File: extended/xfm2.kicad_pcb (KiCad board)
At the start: 2 copper layers, 178.1 x 70.6 mm, 63 parts, among them J1 Midi In, J2 Pin Breakout, J3 Midi Out, J4 Midi Thru, J5 Conn_Coaxial, J6 Jack-DC, J7 A-100_Bus_Connector, J8 AudioJack2, J9 AudioJack2, U1 H11L1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

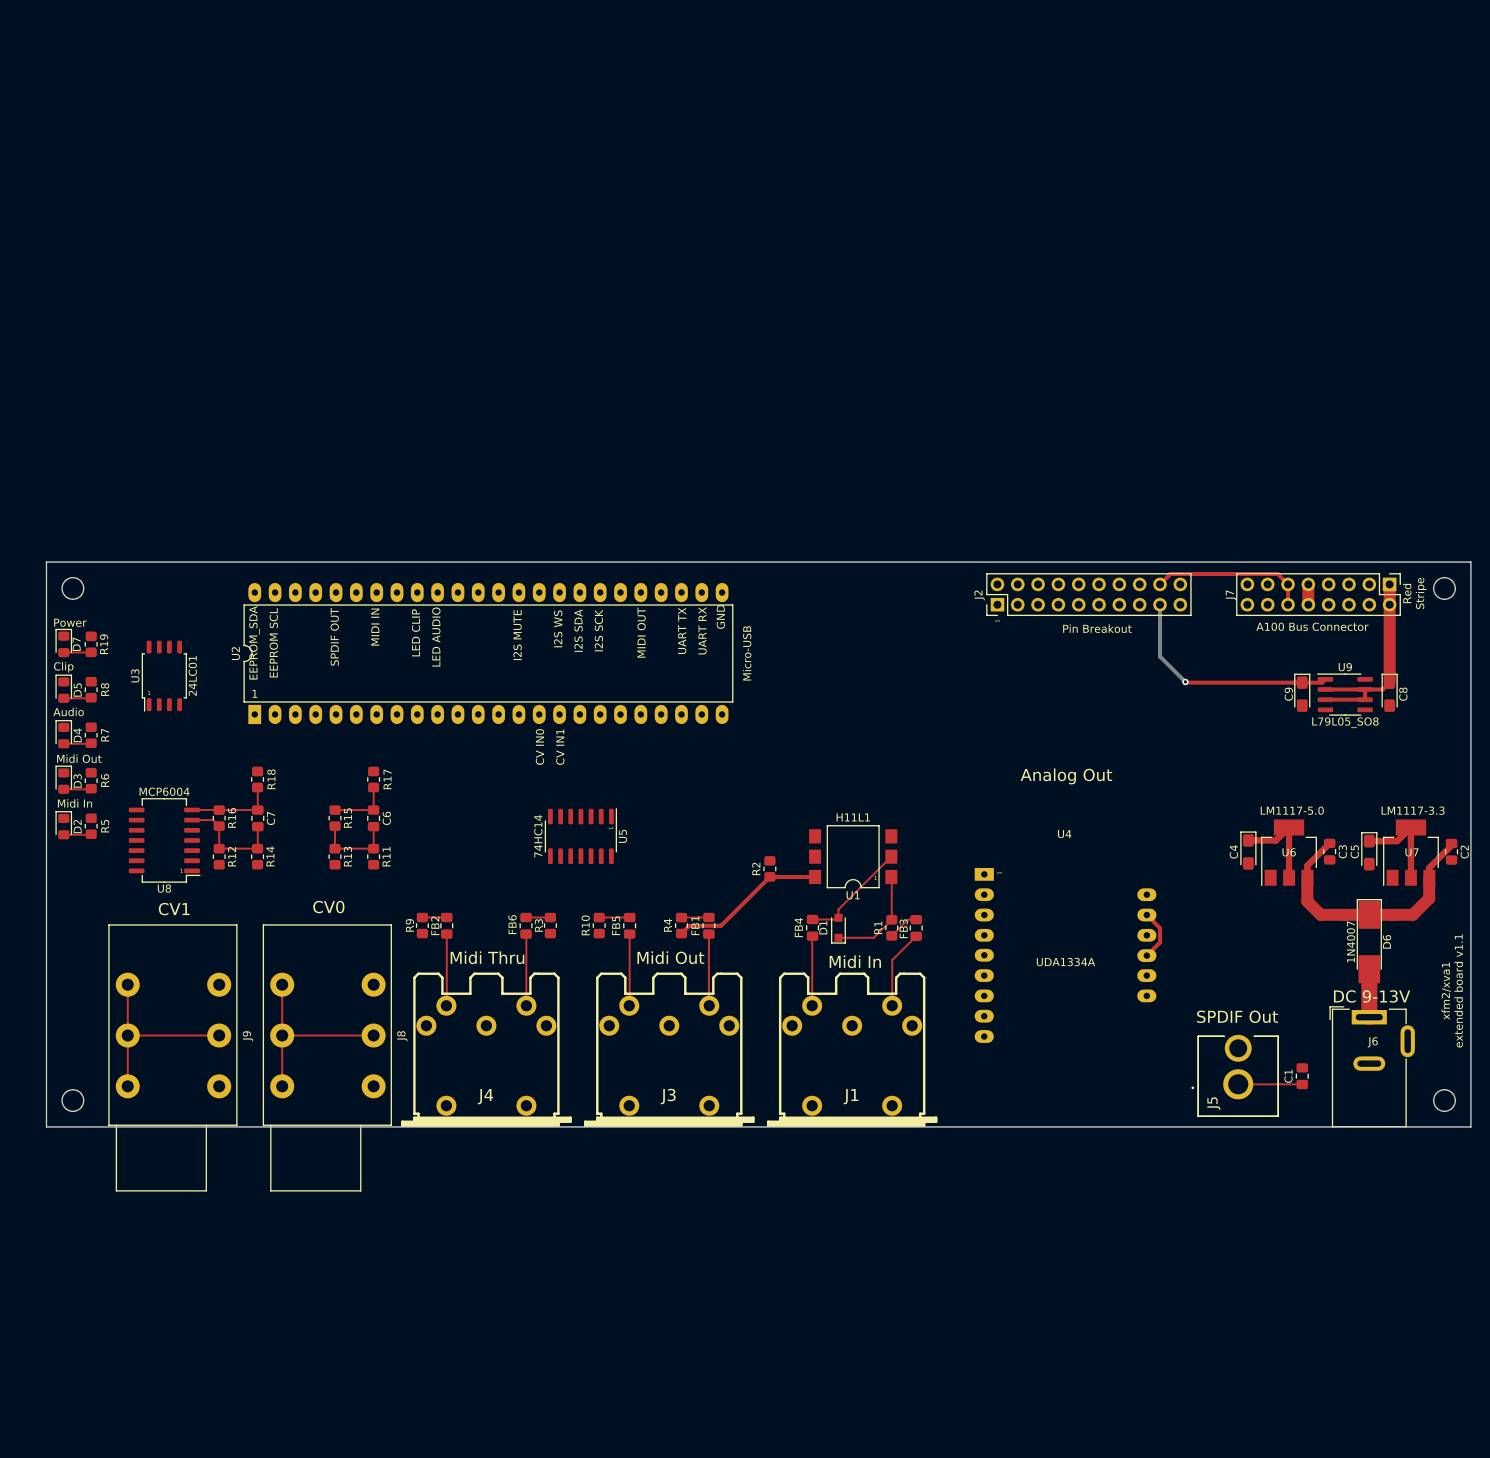
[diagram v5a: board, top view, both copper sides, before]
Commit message: fitted the 6.35mm audio jack which was too small. Added gerbers. ERC seems fine.
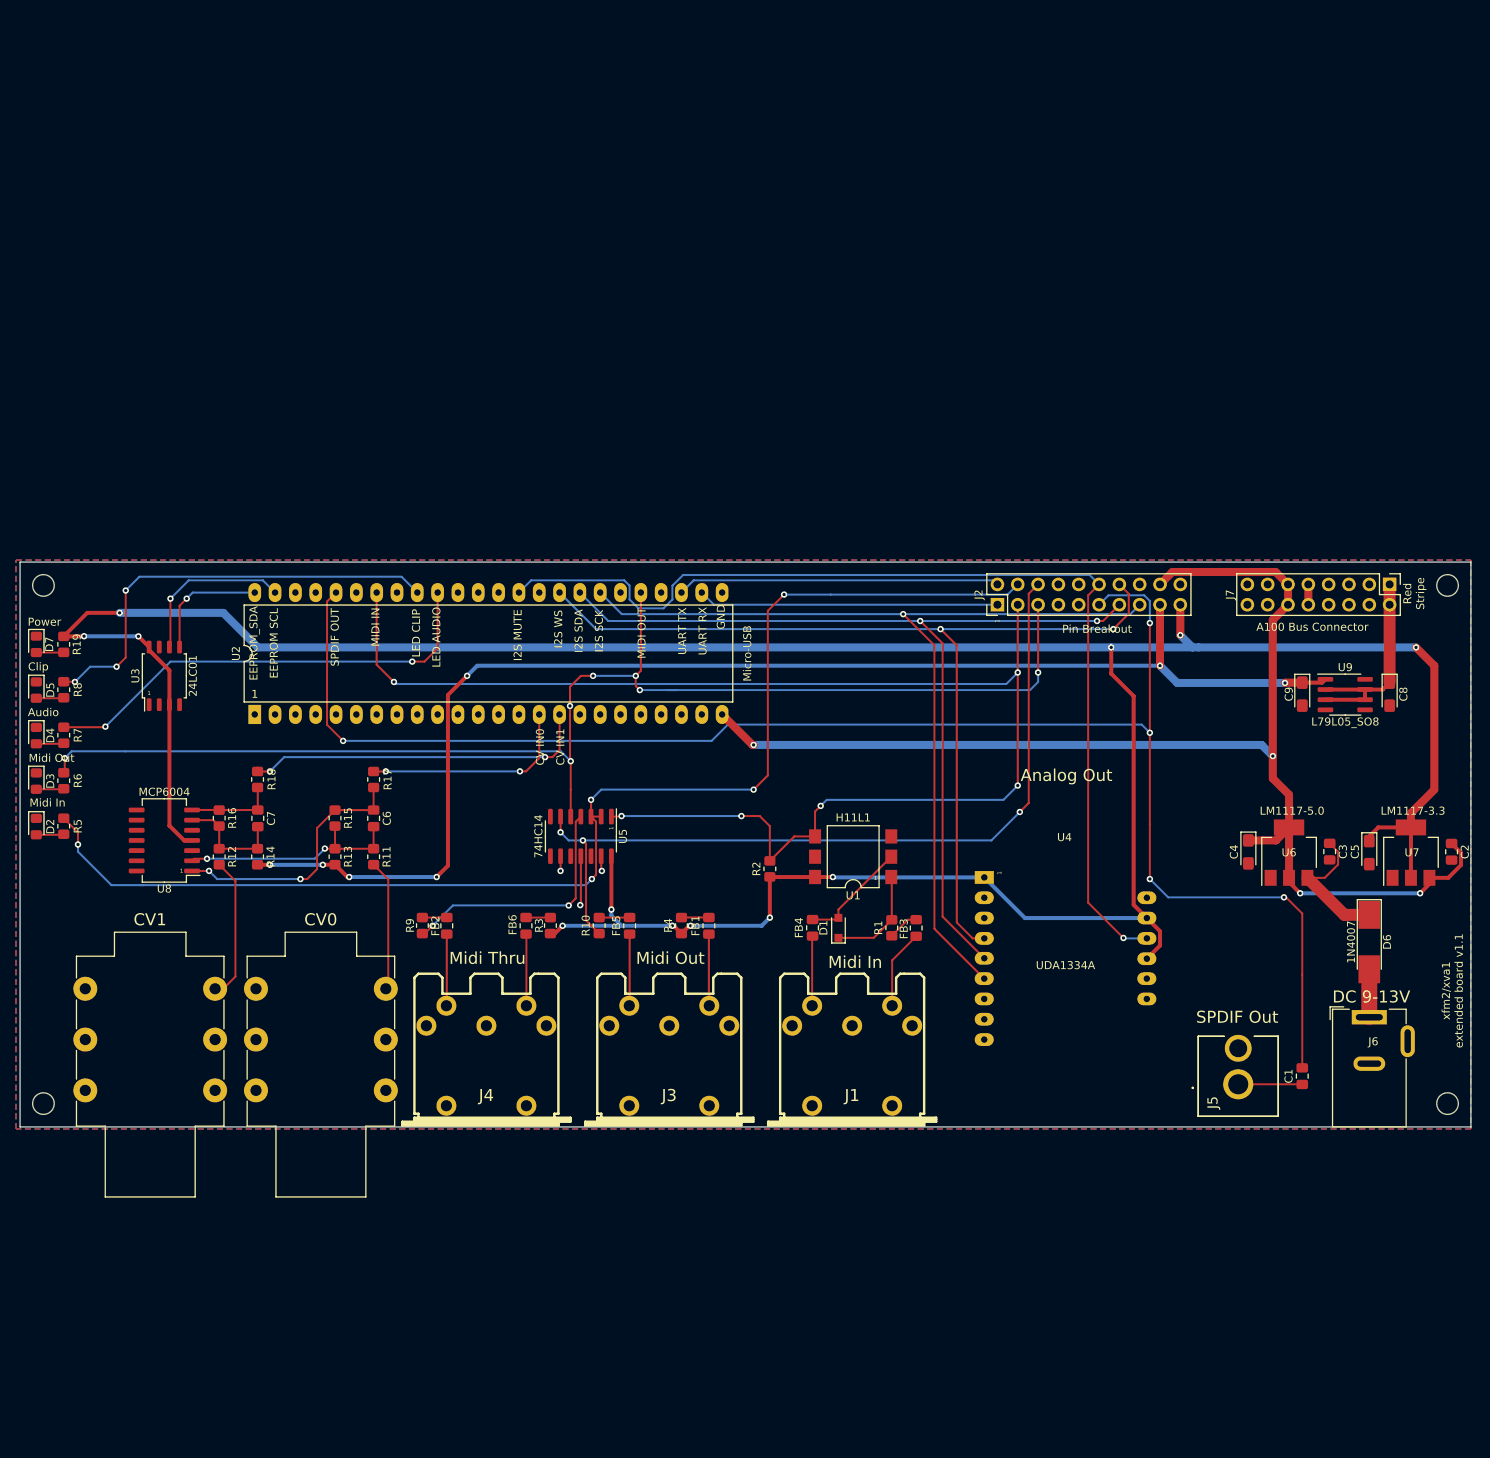
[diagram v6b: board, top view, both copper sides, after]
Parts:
- removed the REF** at (239.5, 87.4)
- removed the REF** at (239.5, 151.4)
- removed the REF** at (68.1, 151.4)
- removed the REF** at (68.1, 87.4)
- added REF**: MountingHole_2.7mm_M2.5_ISO7380, MountingHole:MountingHole_2.7mm_M2.5_ISO7380, F.Cu at (239.9, 87.0)
- added REF**: MountingHole_2.7mm_M2.5_ISO7380, MountingHole:MountingHole_2.7mm_M2.5_ISO7380, F.Cu at (239.9, 151.8)
- added REF**: MountingHole_2.7mm_M2.5_ISO7380, MountingHole:MountingHole_2.7mm_M2.5_ISO7380, F.Cu at (64.4, 151.8)
- added REF**: MountingHole_2.7mm_M2.5_ISO7380, MountingHole:MountingHole_2.7mm_M2.5_ISO7380, F.Cu at (64.4, 87.0)
- D7: value LED_CLIP -> LED_POWER
- J8, J9: footprint Connector_Audio:Jack_6.35mm_Neutrik_NRJ6HM-1_Horizontal -> xfm2:Jack_6.35mm_Neutrik_NMJ6HFD2_Horizontal-ST-only
- moved D2 3.43 mm to (63.5, 117.1)
- moved D3 3.43 mm to (63.5, 111.5)
- moved D4 3.43 mm to (63.5, 105.8)
- moved D5 3.43 mm to (63.5, 100.1)
- moved D7 3.43 mm to (63.5, 94.4)
- moved R19 3.43 mm to (66.9, 94.4)
- moved R5 3.43 mm to (66.9, 117.1)
- moved R6 3.43 mm to (66.9, 111.4)
- moved R7 3.43 mm to (66.9, 105.7)
- moved R8 3.43 mm to (66.9, 100.0)
- moved J8 1.61 mm to (107.2, 137.4)
- moved J9 0.72 mm to (85.9, 137.4)
- moved U4 0.38 mm to (182.0, 118.4)
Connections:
- C2 pad 1: Net-(C2-Pad1) -> +5V
- C3 pad 1: Net-(C2-Pad1) -> Net-(C3-Pad1)
- D6 pad 1: Net-(C2-Pad1) -> Net-(C3-Pad1)
- J8 pad S: Net-(J8-PadS) -> GND
- J8 pad T: GND -> Net-(J8-PadT)
- J9 pad S: Net-(J9-PadS) -> GND
- J9 pad T: GND -> Net-(J9-PadT)
- R11 pad 2: Net-(J8-PadS) -> Net-(J8-PadT)
- R12 pad 2: Net-(J9-PadS) -> Net-(J9-PadT)
- U6 pad 3: Net-(C2-Pad1) -> Net-(C3-Pad1)
- U7 pad 3: Net-(C2-Pad1) -> +5V
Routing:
- net +3V3: track 38.3 -> 388.4 mm, vias 0 -> 12
- net SPDIF_OUT: track 0.00 -> 204.0 mm, vias 0 -> 5
- net MIDI_IN: track 0.00 -> 174.8 mm, vias 0 -> 6
- net MIDI_OUT: track 0.00 -> 164.6 mm, vias 0 -> 7
- net MIDI_IN_INV: track 0.00 -> 159.9 mm, vias 0 -> 5
- net -5V: track 28.7 -> 166.3 mm, vias 1 -> 7
- net +5V: track 31.7 -> 160.6 mm, vias 0 -> 4
- net I2S_MUTE: track 0.00 -> 128.4 mm, vias 0 -> 1
- net I2S_WS: track 0.00 -> 119.8 mm, vias 0 -> 2
- net I2S_SCK: track 0.00 -> 118.8 mm, vias 0 -> 1
- net I2S_SDA: track 0.00 -> 115.2 mm, vias 0 -> 2
- net MIDI_OUT_INV: track 0.00 -> 103.1 mm, vias 0 -> 3
- net LED_AUDIO: track 0.00 -> 57.8 mm, vias 0 -> 2
- net LED_CLIP: track 0.00 -> 55.4 mm, vias 0 -> 3
- net (no net): track 48.3 -> 0.00 mm
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- added copper zone on B.Cu, net GND
- added copper zone on F.Cu, net GND
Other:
- board size 178.1 x 70.6 mm -> 181.4 x 70.6 mm

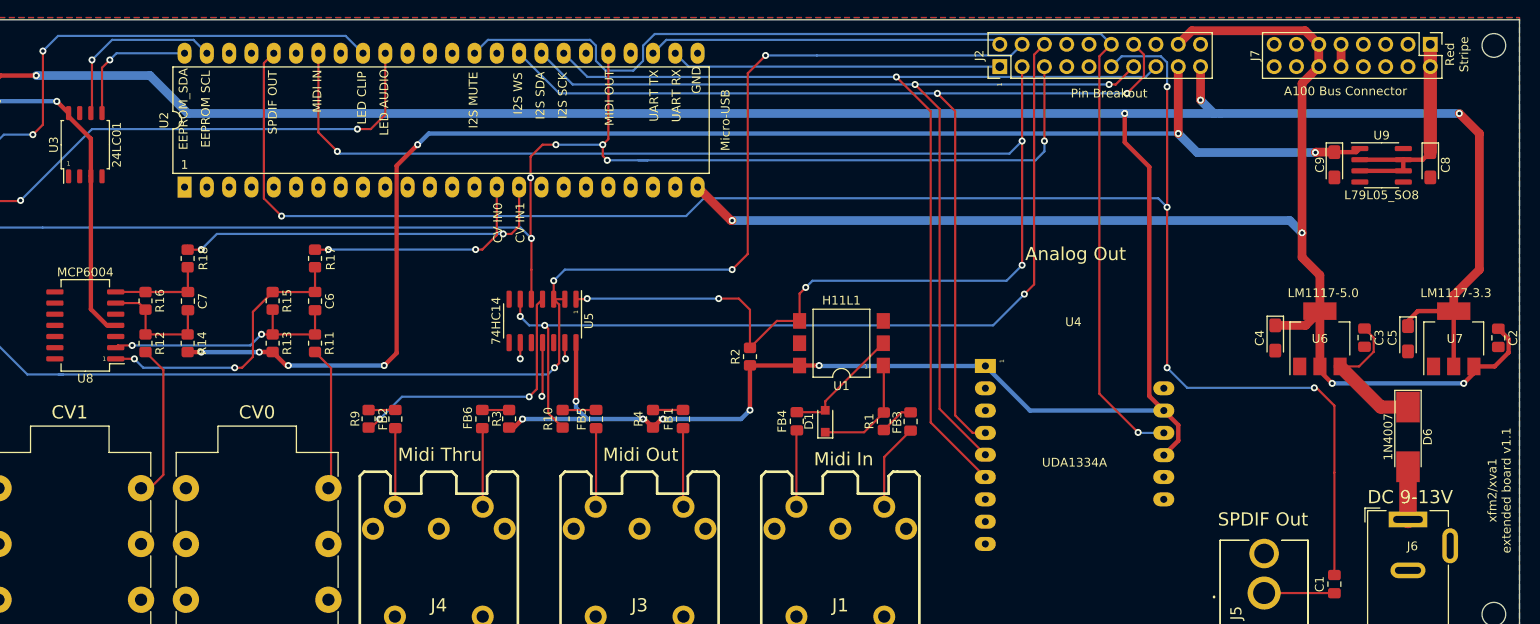
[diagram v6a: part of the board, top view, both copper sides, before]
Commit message: updates for the extended xfm2 board: replacement of opamp components, logic level converter 5v<->3.3v and pull ups for uart.
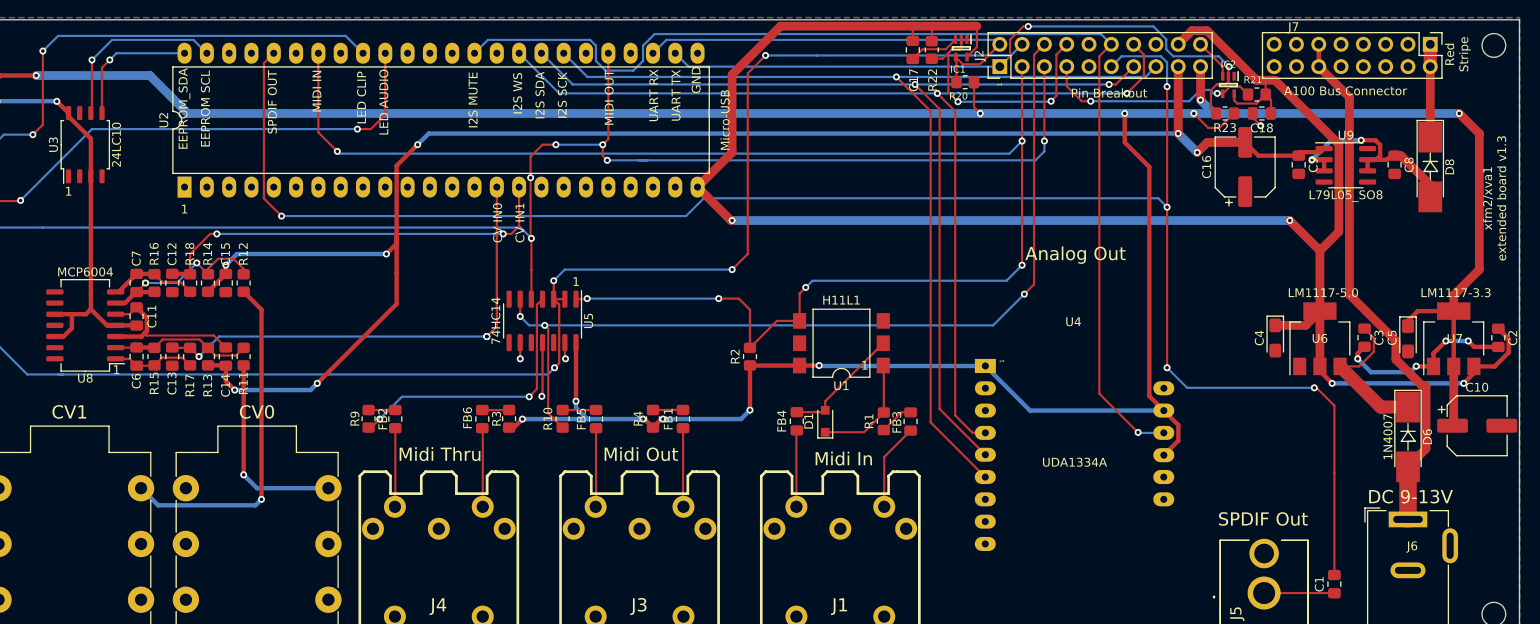
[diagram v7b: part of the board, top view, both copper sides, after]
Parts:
- added C10: 47uF, Capacitor_SMD:CP_Elec_6.3x5.4, F.Cu at (238.0, 130.3)
- added C11: 100nF, Capacitor_SMD:C_0805_2012Metric_Pad1.18x1.45mm_HandSolder, F.Cu at (85.3, 117.9)
- added C12: 100pF, Capacitor_SMD:C_0805_2012Metric_Pad1.18x1.45mm_HandSolder, F.Cu at (89.4, 114.0)
- added C13: 100pF, Capacitor_SMD:C_0805_2012Metric_Pad1.18x1.45mm_HandSolder, F.Cu at (89.4, 122.4)
- added C14: 0.1uF, Capacitor_SMD:C_0805_2012Metric_Pad1.18x1.45mm_HandSolder, F.Cu at (95.5, 122.4)
- added C15: 0.1uF, Capacitor_SMD:C_0805_2012Metric_Pad1.18x1.45mm_HandSolder, F.Cu at (95.5, 114.0)
- added C16: 47uF, Capacitor_SMD:CP_Elec_6.3x5.4, F.Cu at (211.6, 100.8)
- added C17: 100nF, Capacitor_SMD:C_0805_2012Metric_Pad1.18x1.45mm_HandSolder, F.Cu at (173.7, 87.5)
- added C18: 100nF, Capacitor_SMD:C_0805_2012Metric_Pad1.18x1.45mm_HandSolder, F.Cu at (213.5, 94.7)
- added D8: 1N4007, Diode_SMD:D_MELF_Handsoldering, F.Cu at (232.7, 100.8)
- added IC1: 74LVC1G07QSE-7, samacsys:SOT65P210X110-5N, F.Cu at (179.3, 87.3)
- added IC2: 74LVC1G07QSE-7, samacsys:SOT65P210X110-5N, F.Cu at (209.7, 91.5)
- added R20: 10k, Resistor_SMD:R_0805_2012Metric_Pad1.20x1.40mm_HandSolder, F.Cu at (179.7, 91.2)
- added R21: 10k, Resistor_SMD:R_0805_2012Metric_Pad1.20x1.40mm_HandSolder, F.Cu at (212.9, 92.6)
- added R22: 10k, Resistor_SMD:R_0805_2012Metric_Pad1.20x1.40mm_HandSolder, F.Cu at (175.9, 87.5)
- added R23: 10k, Resistor_SMD:R_0805_2012Metric_Pad1.20x1.40mm_HandSolder, F.Cu at (209.3, 94.7)
- C8, C9: footprint Capacitor_Tantalum_SMD:CP_EIA-3216-18_Kemet-A_Pad1.58x1.35mm_HandSolder -> Capacitor_SMD:C_0805_2012Metric_Pad1.18x1.45mm_HandSolder
- D1: value D -> 1N4148
- U3: value 24LC01 -> 24LC10
- moved C6 21.3 mm to (85.3, 122.4), turned to 90 degrees
- moved R17 18.1 mm to (91.4, 122.4)
- moved R15 14.9 mm to (87.4, 122.4), turned to 90 degrees
- moved R12 13.1 mm to (97.5, 114.0)
- moved R11 8.27 mm to (97.5, 122.4)
- moved R13 7.52 mm to (93.5, 122.4)
- moved R14 7.24 mm to (93.5, 114.0)
- moved C7 6.20 mm to (85.3, 114.0)
- moved C8 4.06 mm to (228.6, 100.6)
- moved C9 4.06 mm to (217.7, 100.6)
- moved U9 4.06 mm to (223.1, 100.6)
- moved R18 2.81 mm to (91.4, 114.0)
- moved R16 2.27 mm to (87.4, 114.0)
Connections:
- net UART_RX renamed UART_TX_3.3V
- net UART_TX renamed UART_RX_3.3V
- C8 pad 1: -12V -> Net-(C8-Pad1)
- D6 pad 2: Net-(D6-Pad2) -> 5V-In
- J2 pad 7: Net-(J2-Pad7) -> UART_TX_5V
- J2 pad 8: Net-(J2-Pad8) -> UART_RX_5V
- J6 pad 1: Net-(D6-Pad2) -> 5V-In
- J7 pad 10: +12V -> Net-(J7-Pad10)
- J7 pad 11: +5V -> 5V-In
- J7 pad 12: +5V -> 5V-In
- J7 pad 9: +12V -> Net-(J7-Pad9)
- U8 pad 10: Net-(U8-Pad10) -> +3V3
- U8 pad 12: Net-(U8-Pad12) -> +3V3
- U8 pad 13: Net-(U8-Pad13) -> GND
- U8 pad 9: Net-(U8-Pad9) -> GND
- U9 pad 2: -12V -> Net-(C8-Pad1)
- U9 pad 3: -12V -> Net-(C8-Pad1)
- U9 pad 6: -12V -> Net-(C8-Pad1)
- U9 pad 7: -12V -> Net-(C8-Pad1)
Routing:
- net 5V-In: track 0.00 -> 60.2 mm
- net +5V: track 160.6 -> 219.4 mm
- net GND: track 10.6 -> 64.3 mm, vias 3 -> 8
- net UART_TX_3.3V: track 37.6 -> 76.3 mm, vias 0 -> 2
- net UART_RX_5V: track 0.00 -> 28.7 mm, vias 0 -> 2
- net CV0_3.3V: track 26.9 -> 54.7 mm, vias 2 -> 3
- net +3V3: track 388.4 -> 415.6 mm, vias 12 -> 14
- net Net-(C8-Pad1): track 0.00 -> 25.9 mm, vias 0 -> 2
- net UART_TX_5V: track 0.00 -> 25.0 mm, vias 0 -> 2
- net Net-(C6-Pad1): track 32.5 -> 9.54 mm, vias 2 -> 0
- net Net-(J9-PadT): track 17.0 -> 39.3 mm, vias 0 -> 1
- net -5V: track 166.3 -> 185.8 mm
- net -12V: track 26.4 -> 10.6 mm
- net Net-(C6-Pad2): track 28.9 -> 16.1 mm, vias 2 -> 0
- net UART_RX_3.3V: track 40.3 -> 49.6 mm
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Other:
- board text added: "xfm2/xva1 extended board v1.3"
- board text removed: "xfm2/xva1 extended board v1.1"

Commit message: xfm2/xva pcb version 1.3 (untested, don't use yet).
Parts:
- added C19: 10nF, Capacitor_SMD:C_0805_2012Metric_Pad1.18x1.45mm_HandSolder, F.Cu at (192.5, 135.4)
- added D9: 1N5819/SS14, Diode_SMD:D_SMA-SMB_Universal_Handsoldering, F.Cu at (226.1, 132.1)
- added J10: 10137062-00021LF, samacsys:CONN_10137062-00021LF, F.Cu at (193.5, 147.3)
- added R24: 5.1k, Resistor_SMD:R_0805_2012Metric_Pad1.20x1.40mm_HandSolder, F.Cu at (188.0, 142.0)
- added R25: 5.1k, Resistor_SMD:R_0805_2012Metric_Pad1.20x1.40mm_HandSolder, F.Cu at (193.5, 142.0)
- added U10: CY7C65213-28PVXI, Package_SO:SSOP-28_5.3x10.2mm_P0.65mm, F.Cu at (192.5, 129.5)
- C10: value 47uF -> 1uF; footprint Capacitor_SMD:CP_Elec_6.3x5.4 -> Capacitor_SMD:C_0805_2012Metric_Pad1.18x1.45mm_HandSolder
- C16: value 47uF -> 0.1uF; footprint Capacitor_SMD:CP_Elec_6.3x5.4 -> Capacitor_SMD:C_0805_2012Metric_Pad1.18x1.45mm_HandSolder
- D6, D8: value 1N4007 -> 1N5819/SS14; footprint Diode_SMD:D_MELF_Handsoldering -> Diode_SMD:D_SMA-SMB_Universal_Handsoldering
- moved C10 42.3 mm to (197.4, 142.0), turned to 180 degrees
- moved C16 41.2 mm to (192.5, 137.4), turned to 0 degrees
- moved D6 3.59 mm to (233.7, 132.1)
- moved D8 0.40 mm to (232.7, 100.4)
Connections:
- net UART_RX_3.3V renamed UART_RX_3.3V_FPGA
- net UART_TX_3.3V renamed UART_TX_3.3V_FPGA
- C10 pad 1: +3V3 -> Net-(C10-Pad1)
- C16 pad 1: GND -> /VBUS
- C16 pad 2: -5V -> GND
- D6 pad 2: 5V-In -> +12V
- J2 pad 17: -5V -> Net-(J2-Pad17)
- J6 pad 1: 5V-In -> Net-(D9-Pad2)
- J7 pad 10: Net-(J7-Pad10) -> +12V
- J7 pad 11: 5V-In -> Net-(J7-Pad11)
- J7 pad 12: 5V-In -> Net-(J7-Pad12)
- J7 pad 9: Net-(J7-Pad9) -> +12V
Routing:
- net -5V: track 185.8 -> 256.6 mm, vias 7 -> 6
- net +12V: track 0.00 -> 69.0 mm, vias 0 -> 1
- net 5V-In: track 60.2 -> 0.00 mm
- net /VBUS: track 0.00 -> 42.3 mm, vias 0 -> 4
- net UART_RX_5V: track 28.7 -> 66.0 mm, vias 2 -> 4
- net GND: track 64.3 -> 101.5 mm
- net UART_TX_5V: track 25.0 -> 60.5 mm
- net Net-(C10-Pad1): track 0.00 -> 19.9 mm, vias 0 -> 2
- net /D+: track 0.00 -> 15.7 mm
- net /D-: track 0.00 -> 15.6 mm
- net Net-(J10-PadB5): track 0.00 -> 15.3 mm, vias 0 -> 2
- net +5V: track 219.4 -> 208.3 mm
- net UART_RX_3.3V_FPGA: track 49.6 -> 59.9 mm, vias 0 -> 2
- net Net-(C8-Pad1): track 25.9 -> 16.4 mm, vias 2 -> 0
- net Net-(D9-Pad2): track 0.00 -> 7.67 mm
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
